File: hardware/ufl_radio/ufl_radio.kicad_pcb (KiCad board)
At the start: 6 copper layers, 46.8 x 62 mm, 134 parts, among them J2 U.FL, J3 Shield, J4 Shield, J5 U.FL, J6 Shield, J7 U.FL, J8 Shield, J9 U.FL, U1 MAX2769B, U2 CS48520AS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

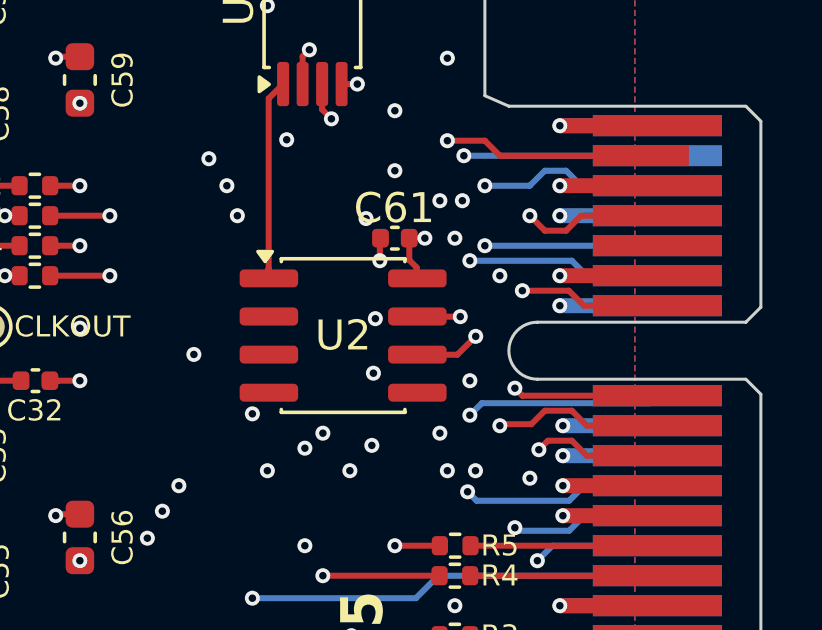
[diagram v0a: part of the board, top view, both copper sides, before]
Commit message: Update to new DFN8 package
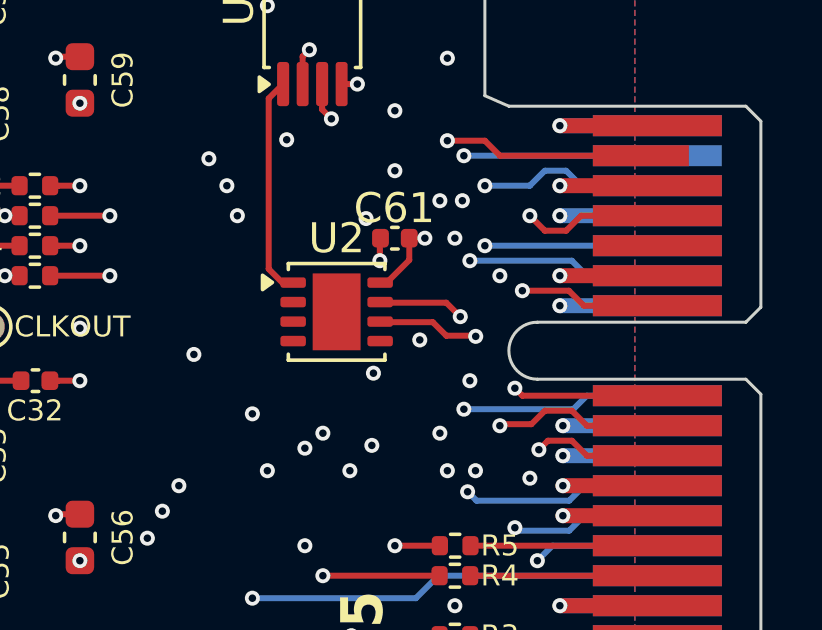
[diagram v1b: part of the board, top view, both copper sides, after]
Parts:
- U2: value CS48520AS -> CS48520AD; footprint Package_SO:SOIC-8_3.9x4.9mm_P1.27mm -> Package_DFN_QFN:DFN-8-1EP_3x3mm_P0.65mm_EP1.6x2.56mm
- moved U2 0.82 mm to (201.1, 95.2)
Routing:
- net Net-(J1-REFCLK+): track 9.91 -> 11.4 mm
- net Net-(J1-REFCLK-): track 11.1 -> 12.4 mm
- net VCC: track 110.6 -> 111.3 mm
- net CLKIN: track 6.69 -> 7.26 mm
